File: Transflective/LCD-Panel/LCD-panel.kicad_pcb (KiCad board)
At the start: 2 copper layers, 154 x 108 mm, 29 parts, among them J1 Conn_02x06_Odd_Even, J2 DS BACKLIGHT, U1 CAP1298

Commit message: Reorganize Transflective directories
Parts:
- added C14: C10uF, Capacitor_SMD:C_0805_2012Metric_Pad1.15x1.40mm_HandSolder, F.Cu at (92.5, -54.1)
- added C15: 10uF, Capacitor_SMD:C_0805_2012Metric_Pad1.15x1.40mm_HandSolder, F.Cu at (92.5, -56.0)
- added TP7: TestPoint, TestPoint:TestPoint_Pad_D1.0mm, F.Cu at (95.4, -53.9)
- added TP8: TestPoint, TestPoint:TestPoint_Pad_D1.0mm, F.Cu at (95.4, -56.0)
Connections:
- J1 pad 10: /DS_K -> GND
- J2 pad K: /DS_K -> GND

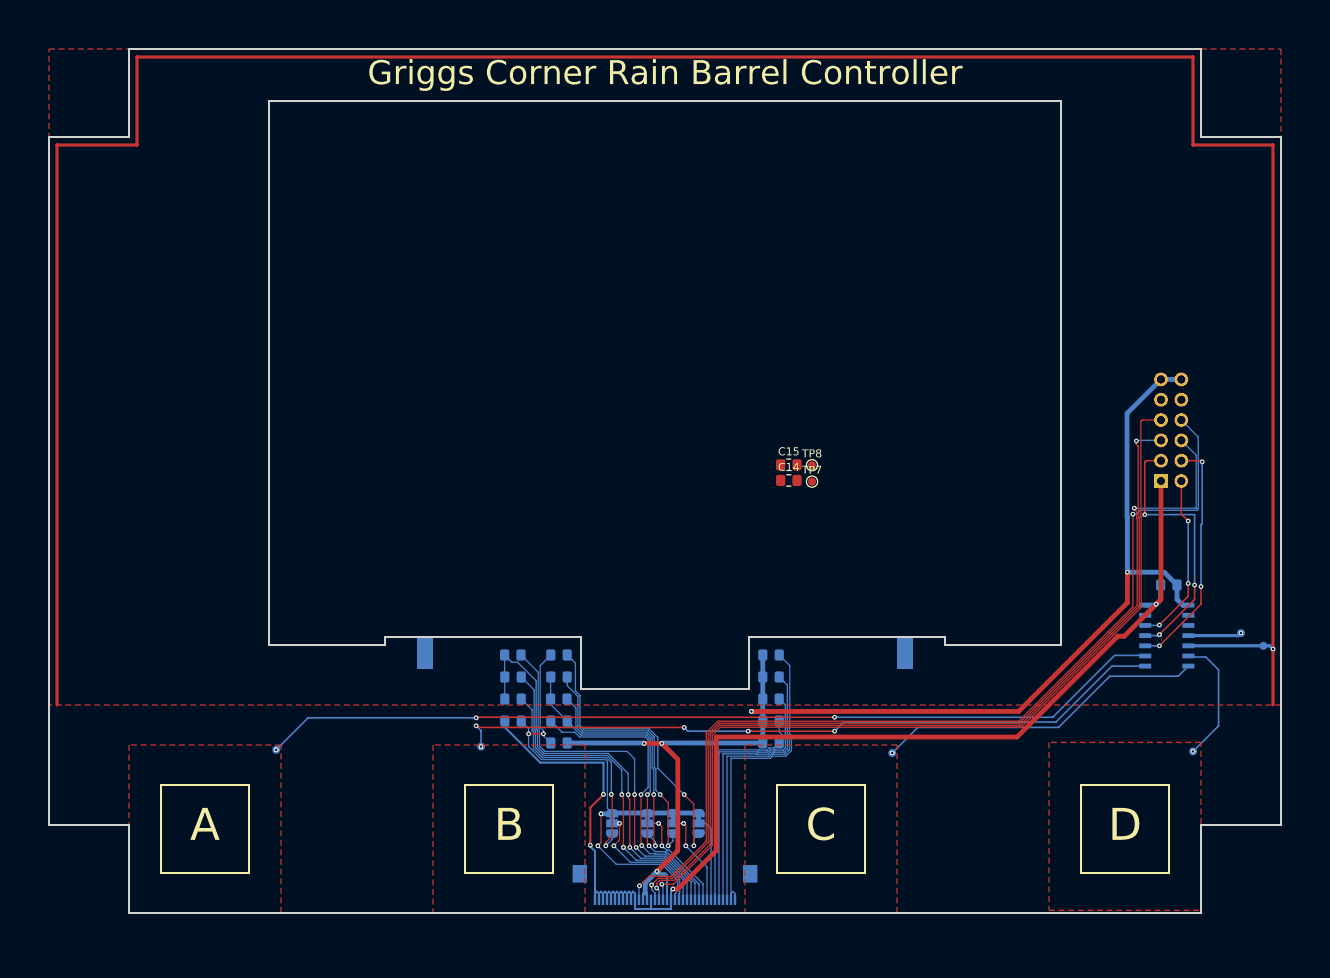
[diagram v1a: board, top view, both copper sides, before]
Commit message: Front panel functionally complete
Still to do: verify orientation of LCD pinout, add 3.3V regulator option
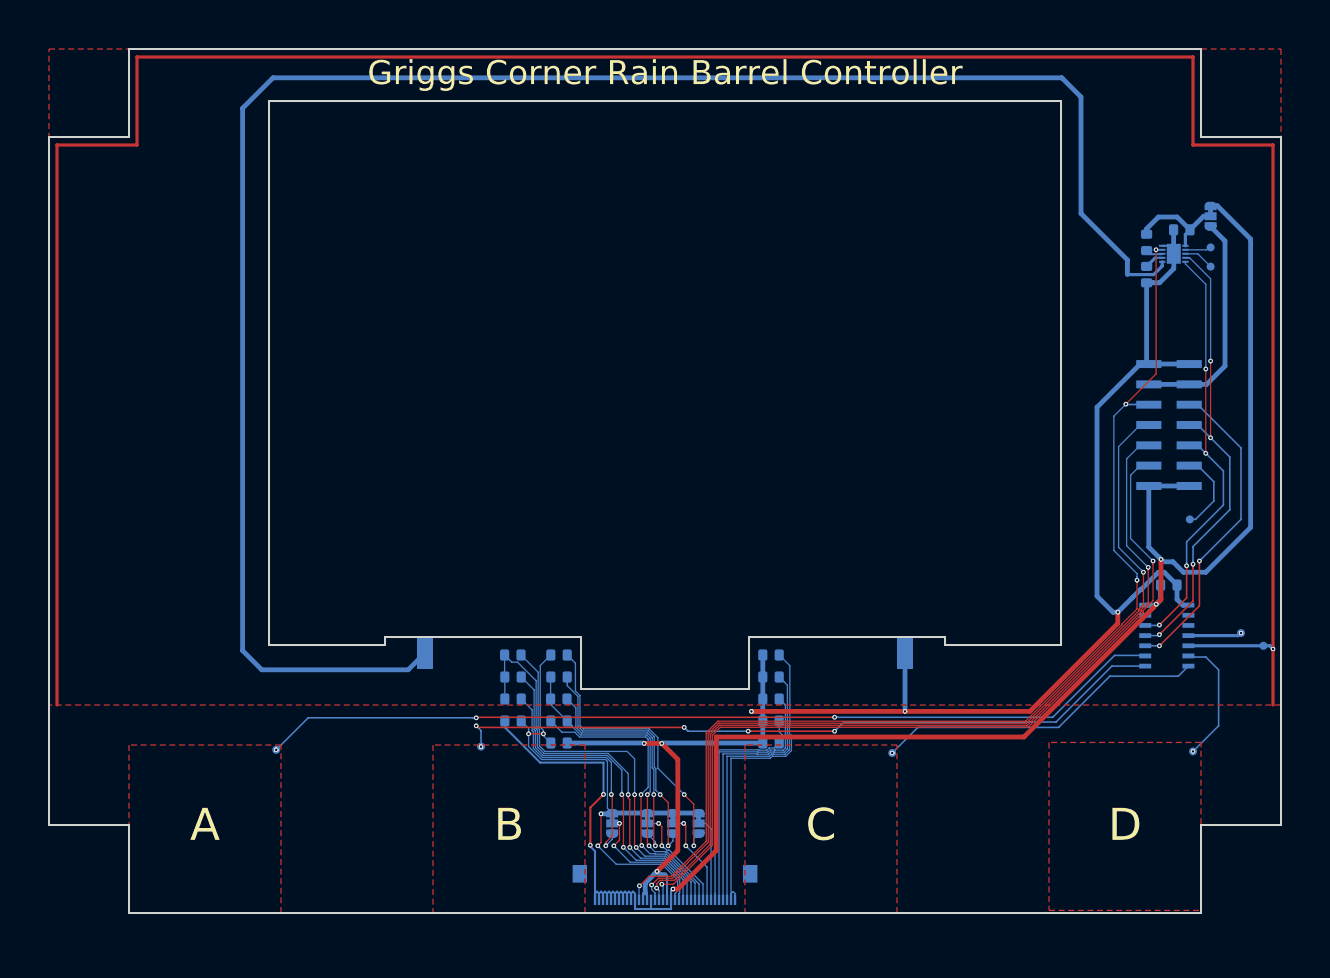
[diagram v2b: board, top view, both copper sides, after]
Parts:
- added JP5: LED PWR, Jumper:SolderJumper-3_P1.3mm_Bridged12_RoundedPad1.0x1.5mm, B.Cu at (145.2, -87.1)
- added L1: 1.0uH, Inductor_SMD:L_0805_2012Metric_Pad1.15x1.40mm_HandSolder, B.Cu at (137.2, -83.8)
- added TP9: TestPoint, TestPoint:TestPoint_Pad_D1.0mm, B.Cu at (142.6, -49.2)
- added U2: U2, ADP1650:ADP1650ACPZ-R7, B.Cu at (140.6, -82.4)
- C14: value C10uF -> 10uF; moved to B.Cu
- C15, TP7, TP8: moved to B.Cu
- J1: footprint Connector_IDC:IDC-Header_2x06_P2.54mm_Vertical -> Connector_PinHeader_2.54mm:PinHeader_2x07_P2.54mm_Vertical_SMD
- moved C14 58.3 mm to (141.6, -85.4), turned to 180 degrees
- moved TP8 56.8 mm to (145.2, -83.2)
- moved TP7 56.6 mm to (145.2, -80.8)
- moved C15 50.7 mm to (137.2, -79.8), turned to 270 degrees
- moved J1 7.07 mm to (140.0, -61.0)
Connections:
- C14 pad 1: +3V3 -> Net-(C14-Pad1)
- J1 pad 10: GND -> /CAP_ALERT
- J1 pad 11: GND -> +5V
- J1 pad 12: GND -> +5V
- J1 pad 2: /CAP_CLK -> +3V3
- J1 pad 3: /CAP_DAT -> /DS_CS
- J1 pad 4: /CAP_ALERT -> Net-(J1-Pad4)
- J1 pad 6: /DS_DAT -> /CAP_CLK
- J1 pad 7: /DS_CS -> /DS_DAT
- J1 pad 8: /DS_RST -> /CAP_DAT
- J1 pad 9: /DS_A -> /DS_RST
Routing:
- net /DS_A: track 0.00 -> 229.8 mm
- net +3V3: track 161.4 -> 223.4 mm, vias 4 -> 5
- net GND: track 160.6 -> 200.6 mm, vias 5 -> 6
- net /CAP_CLK: track 21.6 -> 55.0 mm, vias 3 -> 4
- net +5V: track 0.00 -> 28.6 mm
- net /CAP_DAT: track 33.5 -> 58.5 mm, vias 3 -> 4
- net /DS_RST: track 117.9 -> 141.1 mm, vias 2 -> 4
- net Net-(C14-Pad1): track 0.00 -> 12.3 mm
- net Net-(J1-Pad4): track 0.00 -> 10.3 mm
- net /CAP_ALERT: track 29.7 -> 39.5 mm, vias 3 -> 2
- net /DS_CS: track 110.2 -> 105.9 mm, vias 1 -> 2
- net Net-(TP7-Pad1): track 0.00 -> 3.53 mm
- net Net-(TP8-Pad1): track 0.00 -> 3.08 mm
- net /DS_DAT: track 114.4 -> 112.0 mm
- net Net-(C15-Pad1): track 0.00 -> 2.40 mm
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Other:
- board text added: "1"
- board text added: "K"

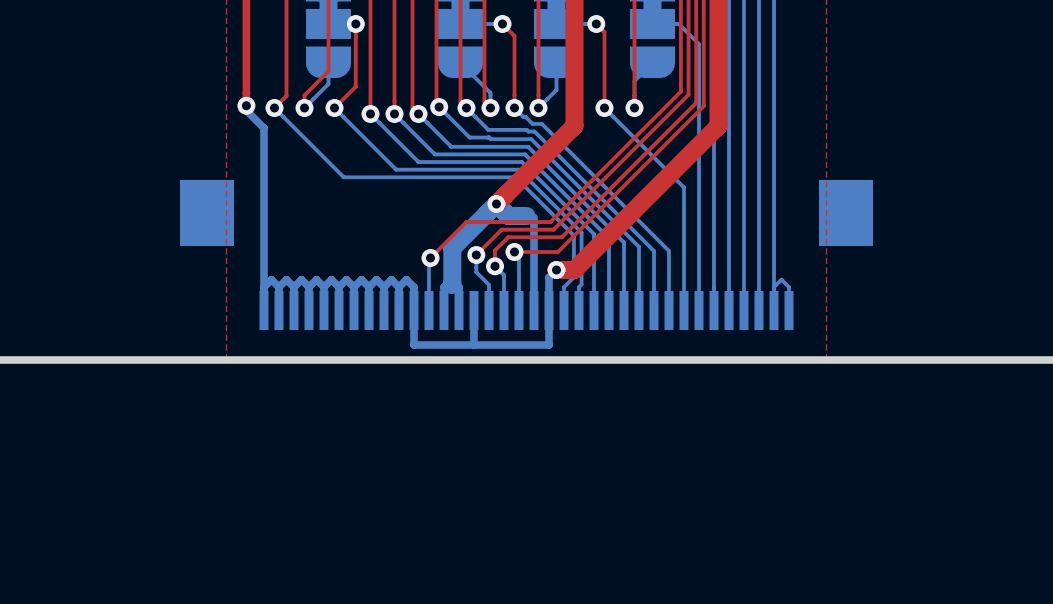
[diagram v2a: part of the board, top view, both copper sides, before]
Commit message: The FPC connector was mirrored :(
Add a vertical FPC connector, with the proper orienatation.  A bunch of
stuff needs to be rerouted.
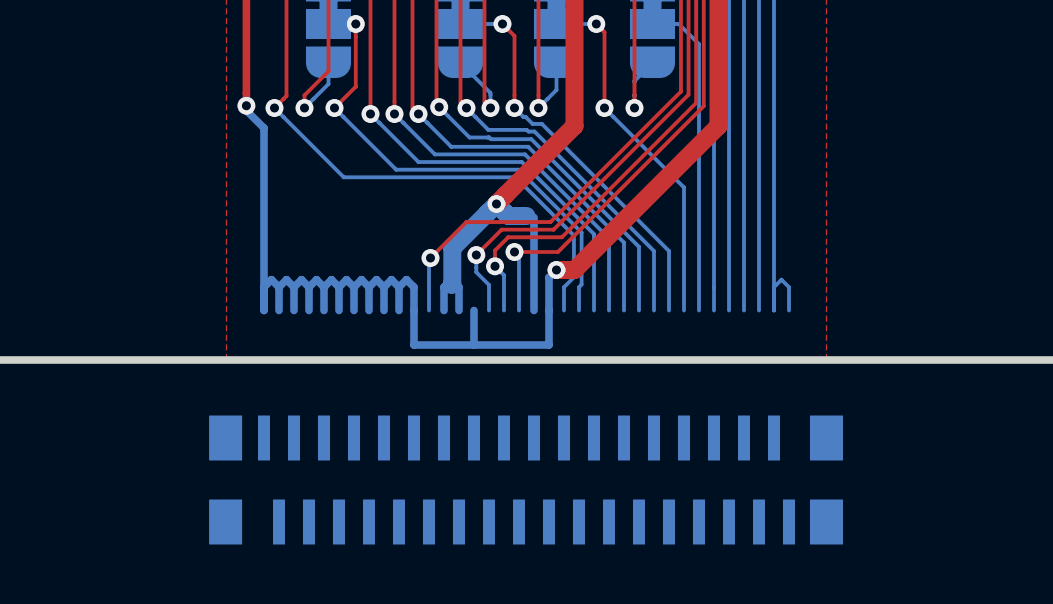
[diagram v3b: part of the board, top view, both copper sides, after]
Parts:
- DS1: footprint Connector_FFC-FPC:Hirose_FH12-36S-0.5SH_1x36-1MP_P0.50mm_Horizontal -> Transflective:F314-1A7H1-11036
- U2: value U2 -> ADP1650ACPZ-R7
- moved DS1 12.1 mm to (86.5, 4.00)

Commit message: Reroute the FPC connector
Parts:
- moved C8 33.4 mm to (66.8, -2.90), turned to 0 degrees
- moved C11 32.0 mm to (75.2, -5.30), turned to 0 degrees
- moved C9 31.7 mm to (75.2, -2.90), turned to 0 degrees
- moved R2 30.2 mm to (81.7, -5.30), turned to 180 degrees
- moved C6 26.6 mm to (71.0, -2.90)
- moved C2 25.7 mm to (81.7, -2.90), turned to 180 degrees
- moved C5 25.5 mm to (81.7, -17.4), turned to 270 degrees
- moved C13 23.5 mm to (71.3, -18.3), turned to 0 degrees
- moved C10 23.3 mm to (71.3, -15.9), turned to 0 degrees
- moved C7 21.7 mm to (71.3, -13.5), turned to 0 degrees
- moved C12 20.1 mm to (71.0, -5.30)
- moved C4 17.2 mm to (78.2, -17.4), turned to 90 degrees
- moved C3 16.4 mm to (74.8, -17.4), turned to 270 degrees
- moved JP4 15.8 mm to (81.6, -22.3)
- moved JP1 15.0 mm to (71.1, -22.3)
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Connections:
- J1 pad 3: /DS_CS -> /DS_RST
- J1 pad 9: /DS_RST -> /DS_CS
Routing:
- net Net-(C11-Pad1): track 46.9 -> 2.88 mm, vias 2 -> 0
- net +3V3: track 223.4 -> 179.5 mm, vias 5 -> 4
- net Net-(C9-Pad1): track 42.9 -> 5.63 mm, vias 2 -> 0
- net Net-(JP1-Pad3): track 37.0 -> 2.63 mm, vias 2 -> 0
- net Net-(C11-Pad2): track 52.4 -> 18.8 mm, vias 2 -> 0
- net Net-(C3-Pad1): track 32.9 -> 2.57 mm, vias 2 -> 0
- net Net-(C12-Pad1): track 37.6 -> 7.25 mm, vias 2 -> 0
- net Net-(C10-Pad1): track 35.7 -> 5.52 mm
- net Net-(C13-Pad1): track 40.5 -> 11.5 mm
- net Net-(C7-Pad1): track 30.7 -> 2.71 mm
- net Net-(C5-Pad1): track 29.9 -> 2.62 mm, vias 2 -> 0
- net Net-(C8-Pad1): track 33.2 -> 6.75 mm
- net Net-(C12-Pad2): track 41.5 -> 16.6 mm, vias 2 -> 0
- net /VLCD: track 65.6 -> 41.2 mm, vias 4 -> 3
- net Net-(C4-Pad1): track 29.7 -> 5.61 mm, vias 2 -> 0
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
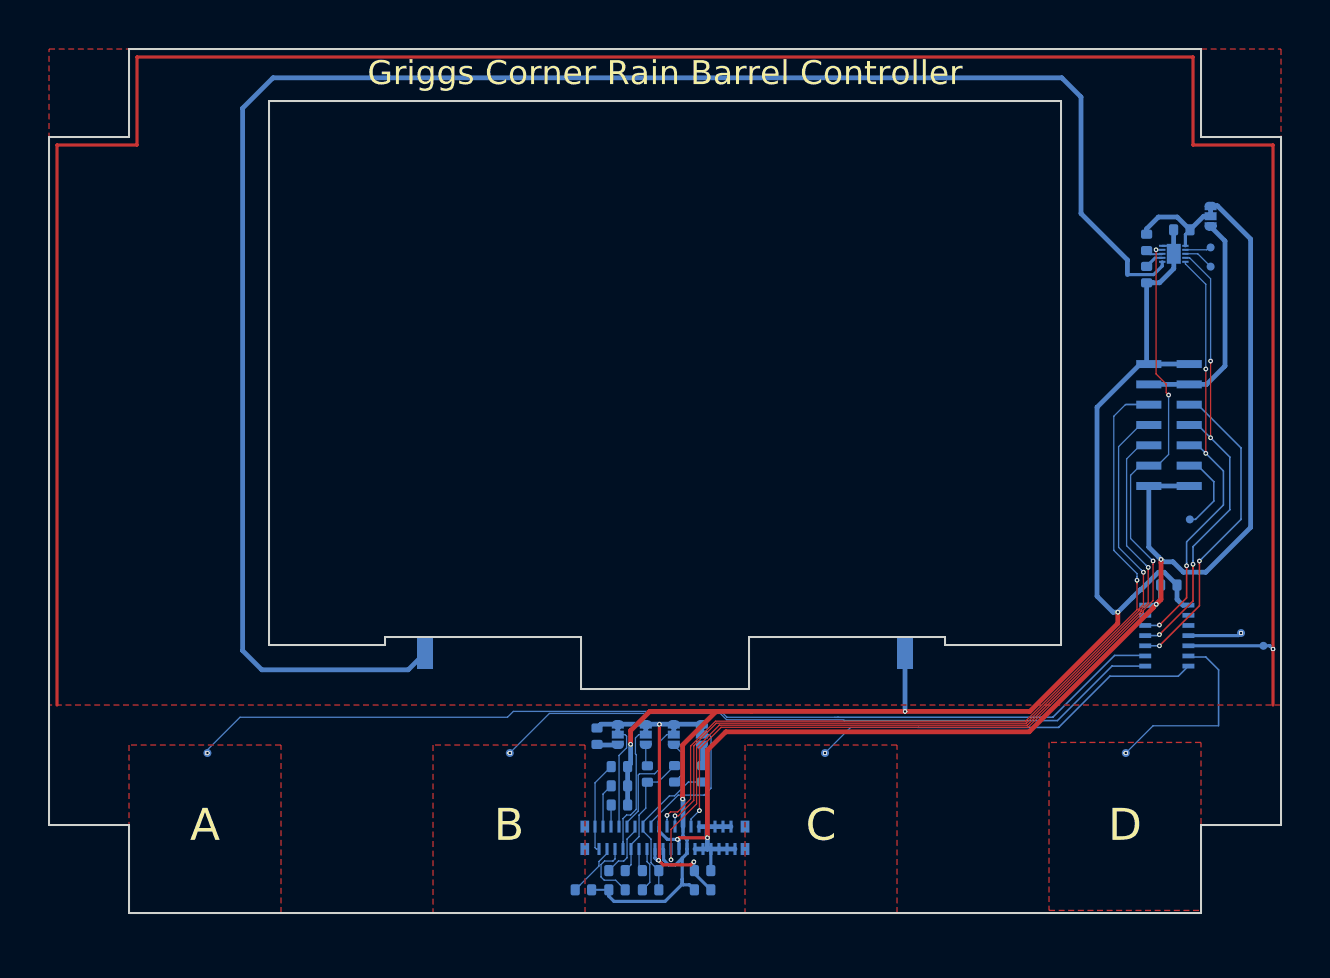
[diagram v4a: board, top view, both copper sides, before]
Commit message: Finish designing front and rear boards for Transflective LCD version
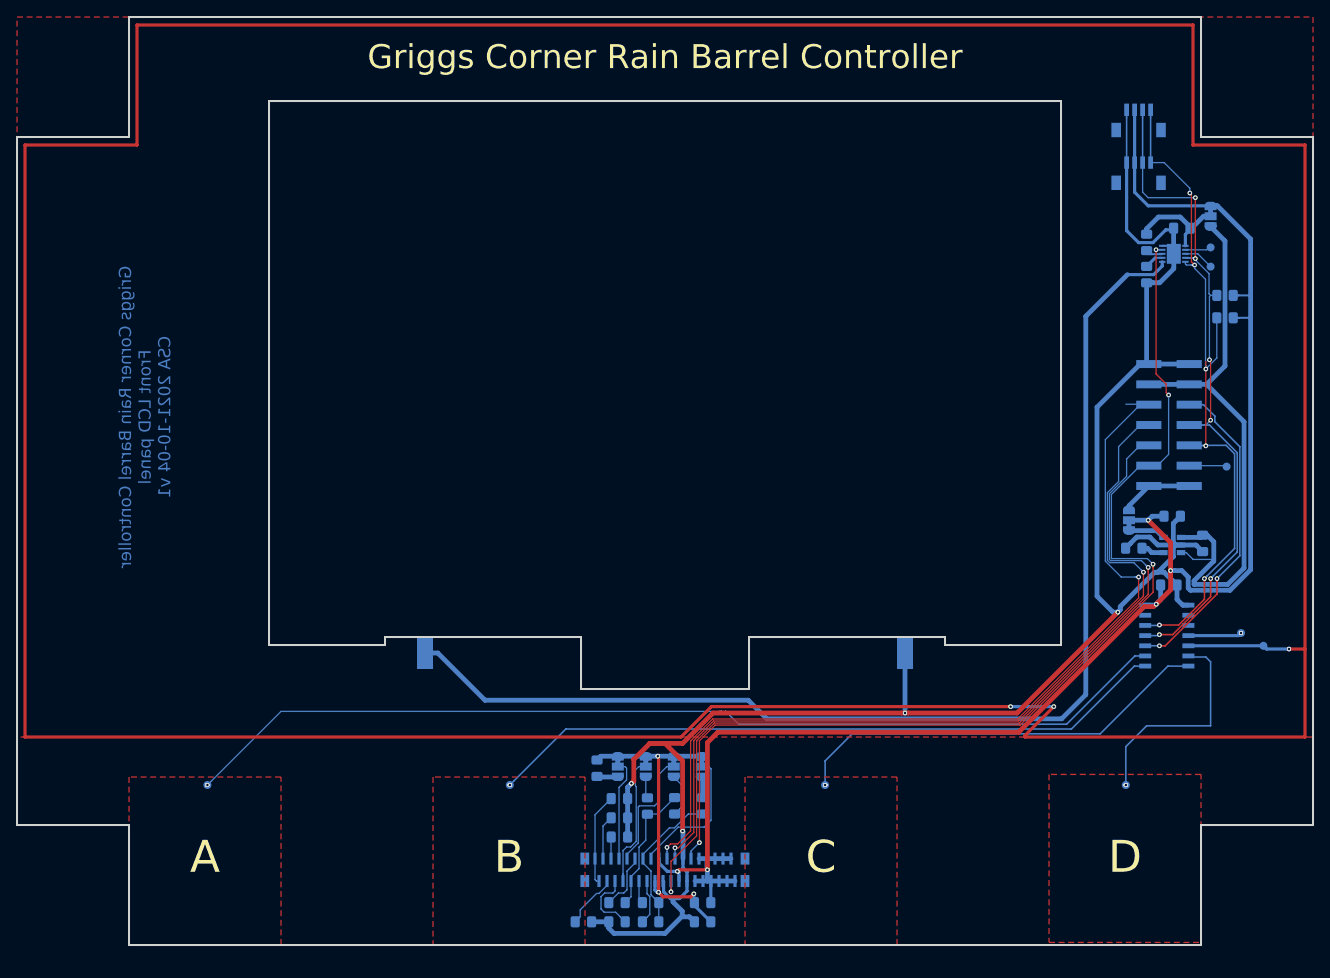
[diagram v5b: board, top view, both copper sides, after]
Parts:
- added C16: .1uF, Capacitor_SMD:C_0805_2012Metric_Pad1.15x1.40mm_HandSolder, B.Cu at (144.2, -46.2)
- added C17: .01uF, Capacitor_SMD:C_0805_2012Metric_Pad1.15x1.40mm_HandSolder, B.Cu at (135.6, -45.6)
- added C18: 1uF, Capacitor_SMD:C_0805_2012Metric_Pad1.15x1.40mm_HandSolder, B.Cu at (140.4, -49.6)
- added J3: STEMMA I2C QT, Transflective:JST-SH-4-VERT-SMD, B.Cu at (136.2, -100.4)
- added J4: STEMMA I2C QT, Transflective:JST-SH-4-VERT-SMD, B.Cu at (136.2, -93.8)
- added JP6: USE LOCAL REG, Jumper:SolderJumper-3_P1.3mm_Bridged12_RoundedPad1.0x1.5mm, B.Cu at (135.0, -49.1)
- added R3: 10k, Resistor_SMD:R_0805_2012Metric_Pad1.15x1.40mm_HandSolder, B.Cu at (147.0, -74.4)
- added R4: 10k, Resistor_SMD:R_0805_2012Metric_Pad1.15x1.40mm_HandSolder, B.Cu at (147.0, -77.2)
- added U3: AP131-33, Package_TO_SOT_SMD:SOT-23-5, B.Cu at (140.4, -46.0)
- J1: value Conn_02x06_Odd_Even -> To Bottom Board
- TP1: value TestPoint -> GUARD
- TP2: value TestPoint -> A
- TP3: value TestPoint -> B
- TP4: value TestPoint -> C
- TP5: value TestPoint -> D
- TP6: value TestPoint -> PROX
- TP7: value TestPoint -> GPIO1
- TP8: value TestPoint -> GPIO2
- TP9: value TestPoint -> Unused
- moved TP9 8.04 mm to (147.2, -55.8)
- moved C10 4.00 mm to (71.3, -11.9)
- moved C11 4.00 mm to (75.2, -1.30)
- moved C12 4.00 mm to (71.0, -1.30)
- moved C13 4.00 mm to (71.3, -14.3)
- moved C2 4.00 mm to (81.7, 1.10)
- moved C3 4.00 mm to (74.8, -13.4)
- moved C6 4.00 mm to (71.0, 1.10)
- moved C7 4.00 mm to (71.3, -9.50)
- moved C8 4.00 mm to (66.8, 1.10)
- moved C9 4.00 mm to (75.2, 1.10)
- moved DS1 4.00 mm to (86.5, -5.40)
- moved JP1 4.00 mm to (71.1, -18.3)
- moved JP2 4.00 mm to (74.6, -18.3)
- moved JP3 4.00 mm to (78.1, -18.3)
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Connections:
- J1 pad 1: +3V3 -> Net-(J1-Pad1)
- J1 pad 2: +3V3 -> Net-(J1-Pad1)
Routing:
- net /CAP_GUARD: track 324.7 -> 523.2 mm, vias 1 -> 3
- net /DS_A: track 229.8 -> 147.2 mm
- net +5V: track 28.6 -> 75.8 mm
- net GND: track 204.6 -> 248.5 mm
- net /CAP_CLK: track 55.0 -> 91.9 mm, vias 4 -> 6
- net /CAP_DAT: track 58.5 -> 89.1 mm, vias 4 -> 6
- net +3V3: track 179.5 -> 208.6 mm, vias 4 -> 5
- net Net-(J1-Pad1): track 0.00 -> 9.06 mm
- net /DS_RST: track 124.3 -> 132.8 mm
- net /DS_CLK: track 103.3 -> 111.1 mm
- net /DS_DAT: track 100.9 -> 107.4 mm
- net Net-(J1-Pad4): track 10.3 -> 4.72 mm
- net /DS_CS: track 107.9 -> 112.8 mm
- net Net-(JP6-Pad1): track 0.00 -> 4.65 mm
- net /BUTTON_C: track 49.9 -> 53.3 mm
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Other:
- board size 154 x 108 mm -> 162 x 116 mm
- board text added: "Griggs Corner Rain Barrel Controller Front LCD panel CSA 2021-10-04 v1"
- board text added: "JLCJLCJLC"
- board text removed: "5x"
- board text removed: "6x"
- board text removed: "7x"
- board text removed: "VLCD LIMIT"
